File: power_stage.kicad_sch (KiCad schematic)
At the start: 26 parts, among them U7 LMG2100R026VBNR, U8 AD8417

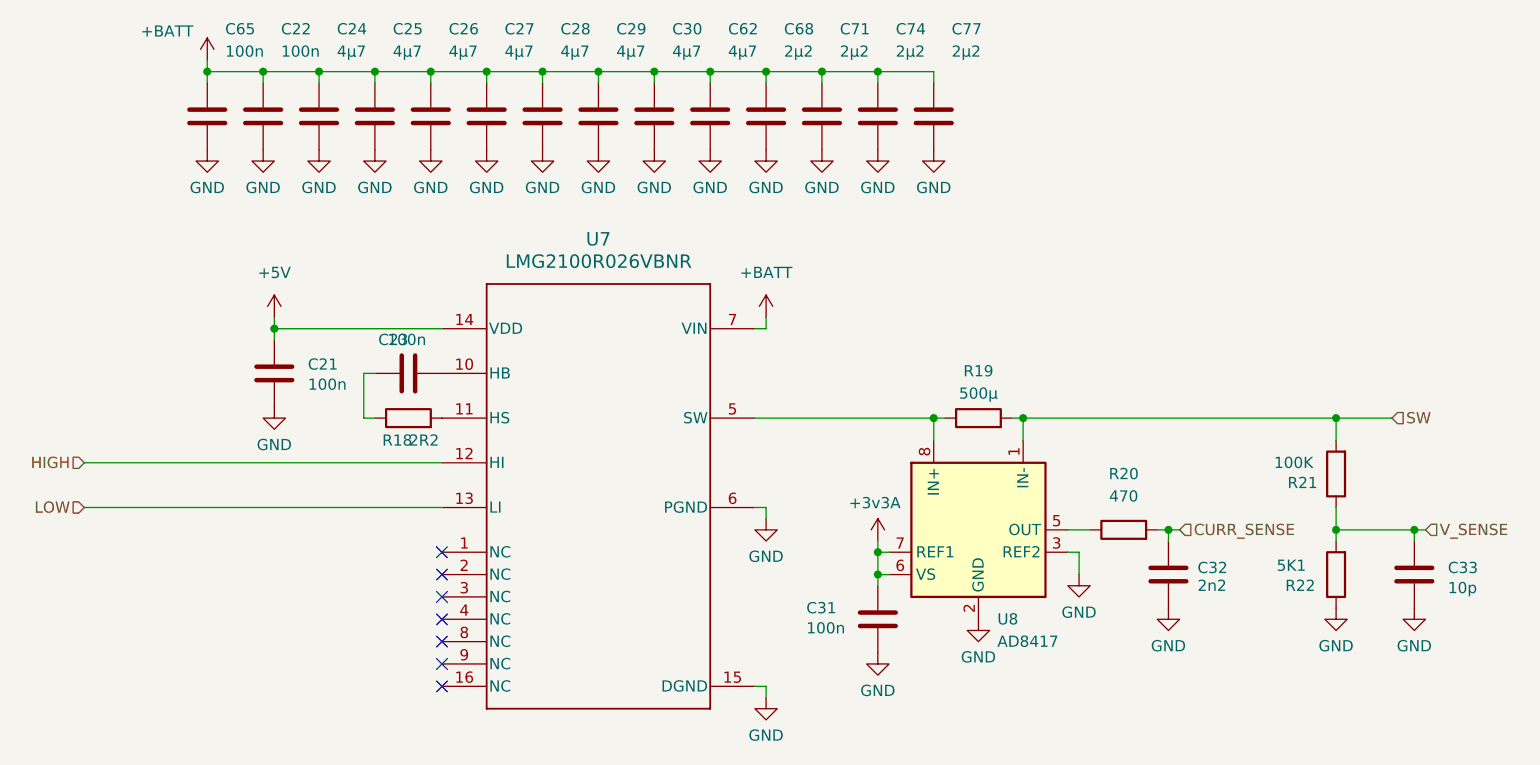
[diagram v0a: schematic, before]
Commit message: Changed Lib link and added BGA part
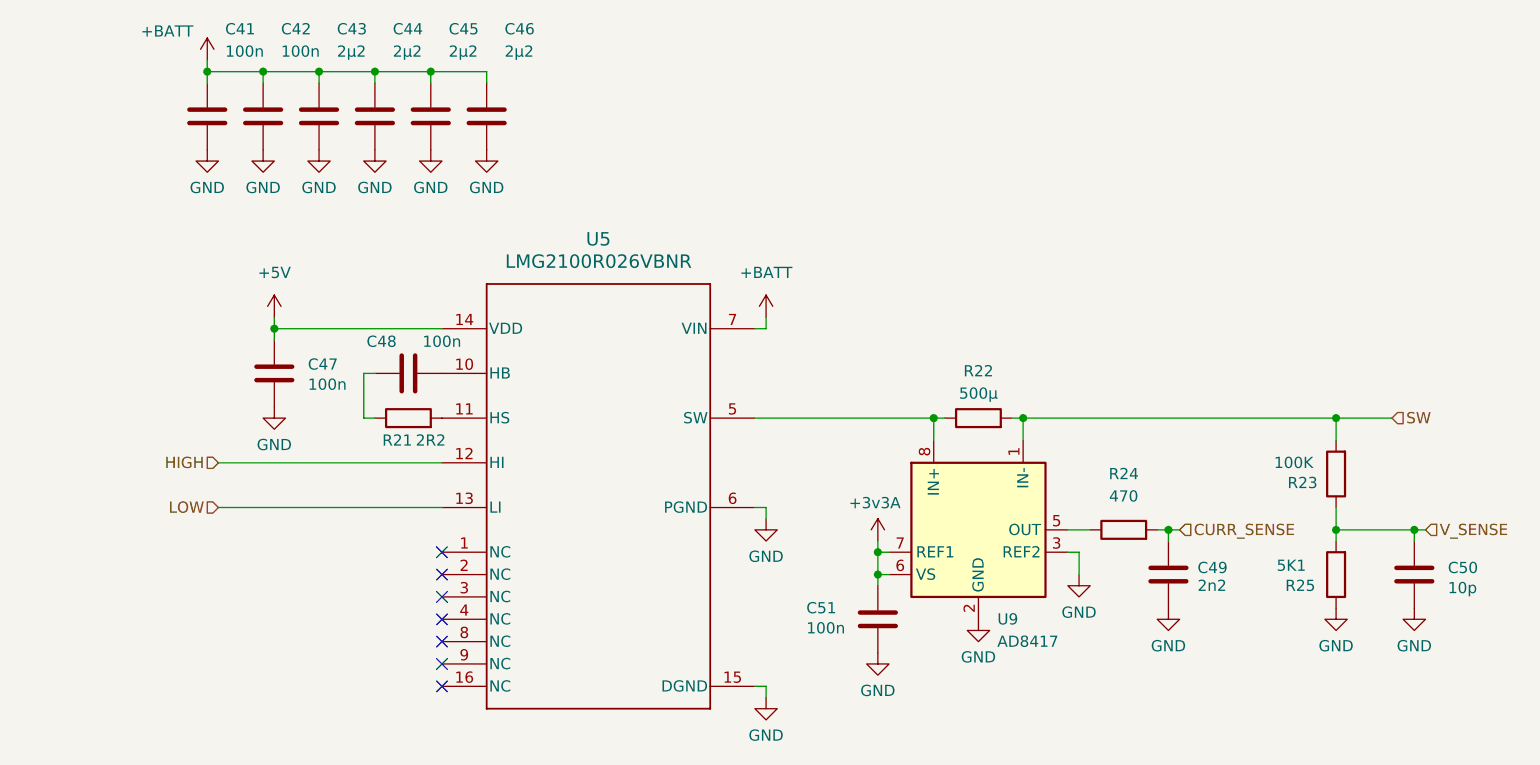
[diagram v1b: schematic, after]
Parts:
- removed C24, C25, C26, C27, C28, C29, C30, C62: 4µ7, Capacitor_SMD:C_1206_3216Metric, symbol Device:C
- removed U7: LMG2100R026VBNR, My Library:VBN0018A-MFG, symbol My Library:LMG2100R026VBNR
- added U5: LMG2100R026VBNR, VBN0018A-MFG, symbol My_Transistor_Half_Bridge:LMG2100R026VBNR
- renumbered C65 to C41, C22 to C42, C68 to C43, C71 to C44, C74 to C45, C77 to C46, C21 to C47, C23 to C48, C32 to C49, C33 to C50, C31 to C51, R18 to R21, R19 to R22, R21 to R23, R20 to R24, R22 to R25, U8 to U9
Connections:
- net +5V: now also U5.14 (VDD)
- net +BATT: now also U5.7 (VIN)
- net GND: now also U5.15 (DGND), U5.6 (PGND)
- net HIGH: now also U5.12 (HI)
- net LOW: now also U5.13 (LI)
- net at C48.2: now also U5.10 (HB)
- net at R22.1, U9.8 (IN+): now also U5.5 (SW)
- net at R21.2: now also U5.11 (HS)
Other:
- moved on the sheet: C43, C44, C45, C46
